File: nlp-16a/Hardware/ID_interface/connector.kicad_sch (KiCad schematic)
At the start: 8 parts

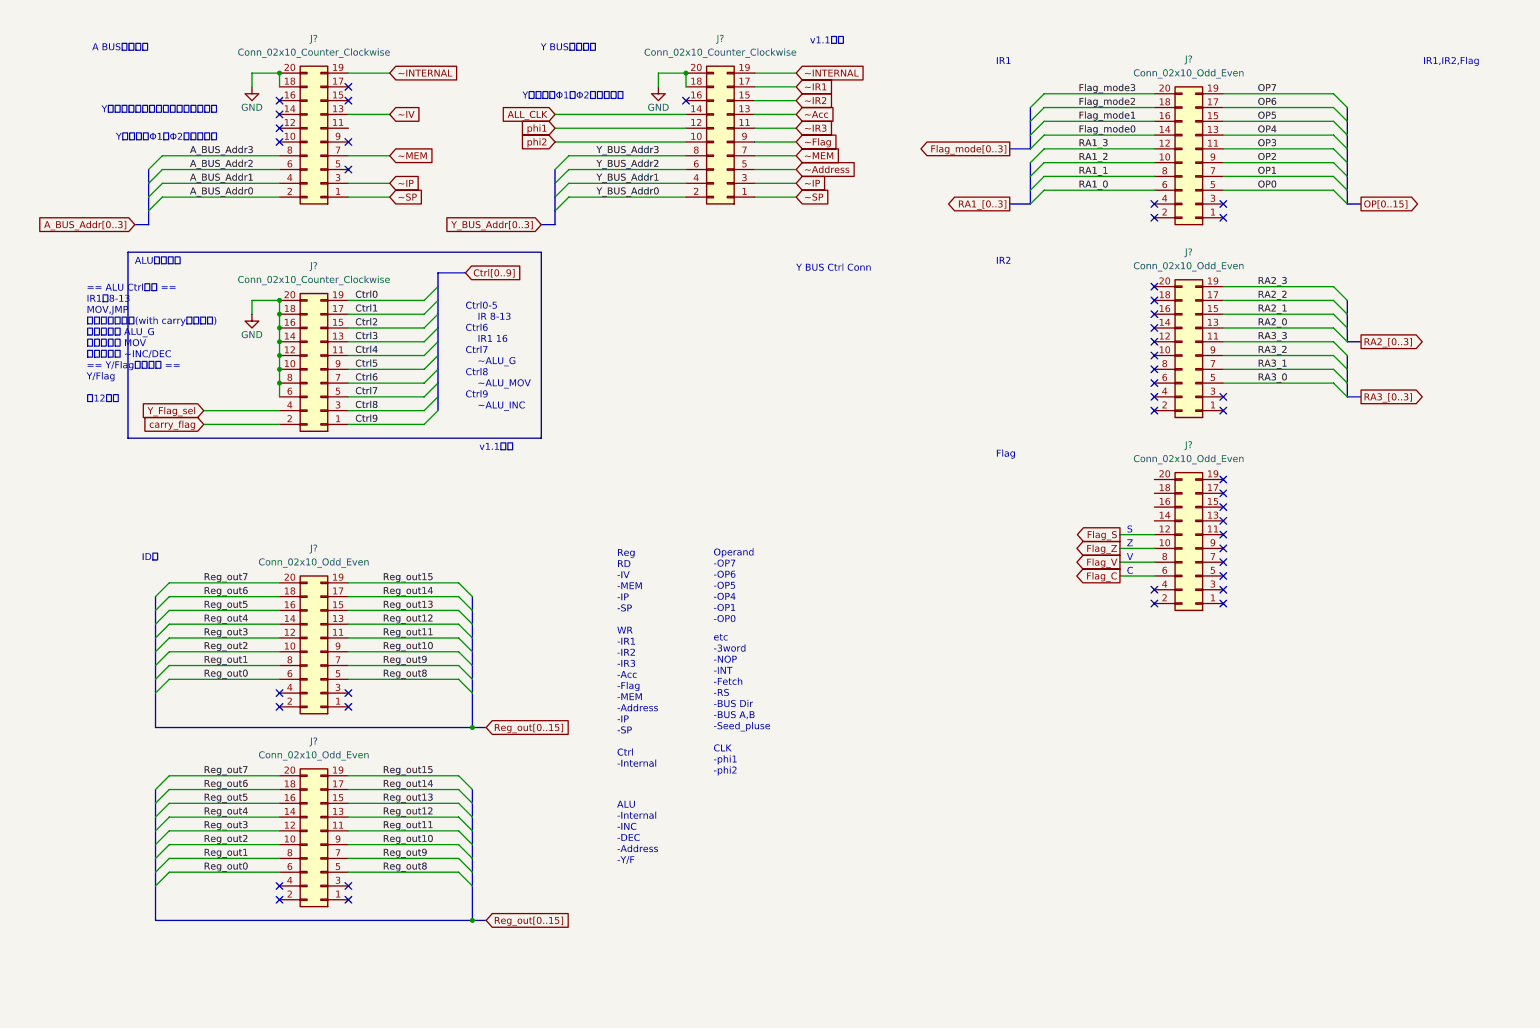
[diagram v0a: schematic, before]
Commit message: 命令デコーダとの配線方法を変更
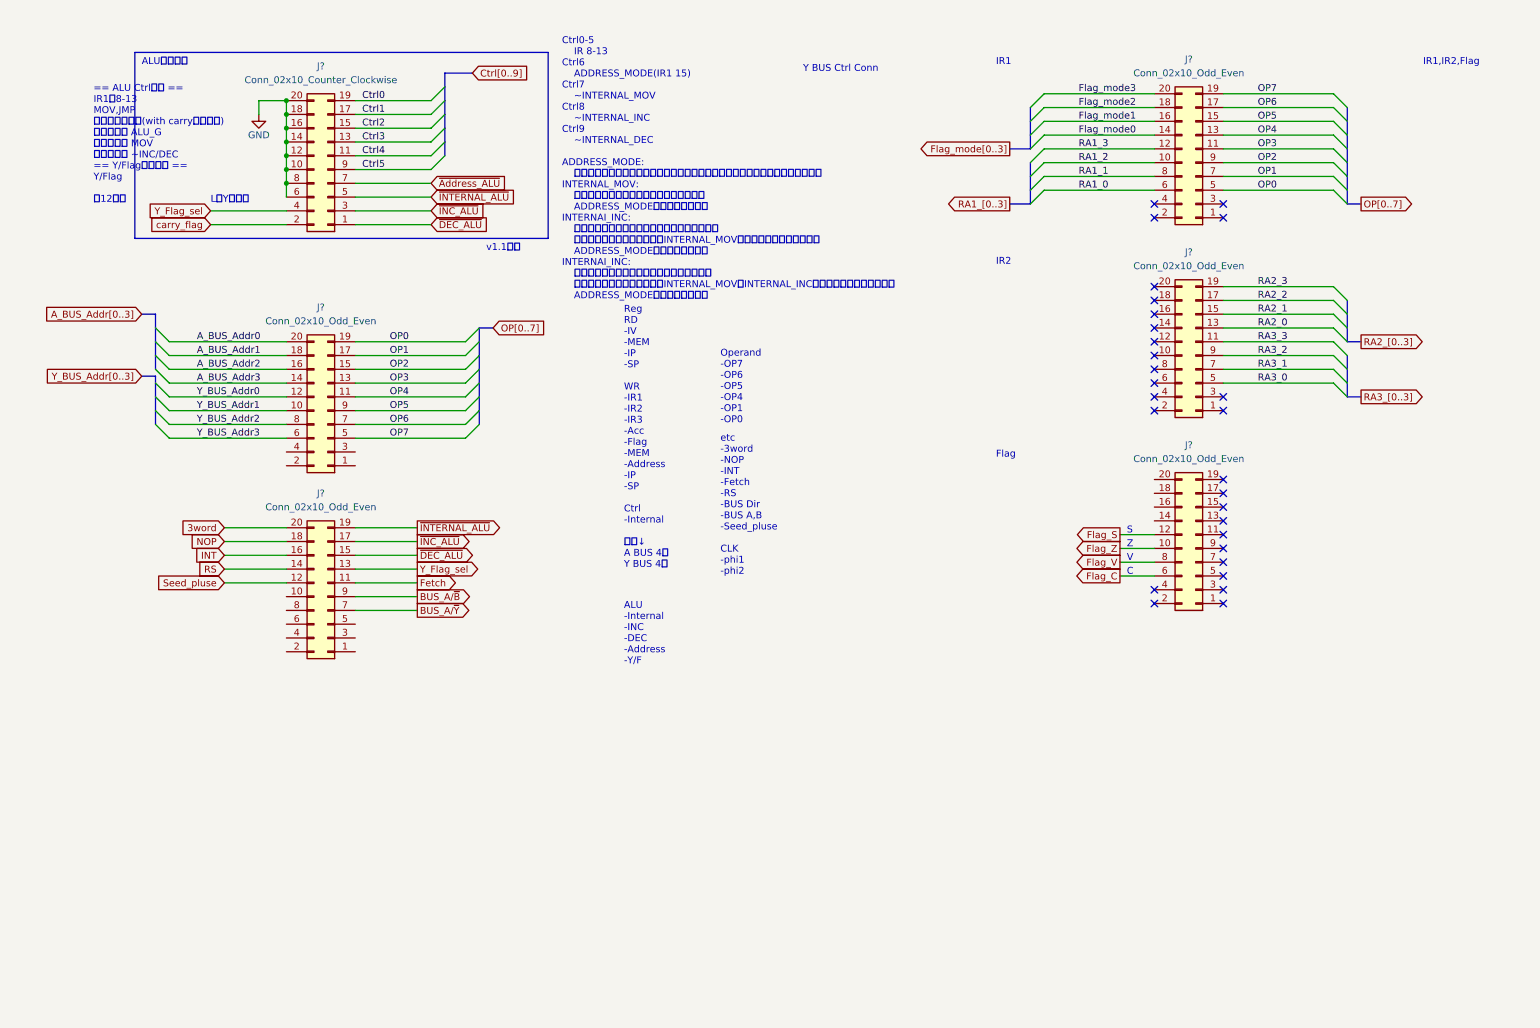
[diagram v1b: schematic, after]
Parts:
- removed J? (x2): Conn_02x10_Counter_Clockwise, Connector_PinHeader_2.54mm:PinHeader_2x10_P2.54mm_Horizontal, symbol Connector_Generic:Conn_02x10_Odd_Even
- removed J? (x2): Conn_02x10_Odd_Even, Connector_PinHeader_2.54mm:PinHeader_2x10_P2.54mm_Horizontal, symbol Connector_Generic:Conn_02x10_Odd_Even
- added J? (x2): Conn_02x10_Odd_Even, Connector_PinHeader_2.54mm:PinHeader_2x10_P2.54mm_Horizontal, symbol Connector_Generic:Conn_02x10_Odd_Even
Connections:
- net A_BUS_Addr0: now also J?.20 (Pin_20)
- net A_BUS_Addr1: now also J?.18 (Pin_18)
- net A_BUS_Addr2: now also J?.16 (Pin_16)
- net A_BUS_Addr3: now also J?.14 (Pin_14)
- net OP0: now also J?.19 (Pin_19)
- net OP1: now also J?.17 (Pin_17)
- net OP2: now also J?.15 (Pin_15)
- net OP3: now also J?.13 (Pin_13)
- net OP4: now also J?.11 (Pin_11)
- net OP5: now also J?.9 (Pin_9)
- net OP6: now also J?.7 (Pin_7)
- net OP7: now also J?.5 (Pin_5)
- net Y_BUS_Addr0: now also J?.12 (Pin_12)
- net Y_BUS_Addr1: now also J?.10 (Pin_10)
- net Y_BUS_Addr2: now also J?.8 (Pin_8)
- net Y_BUS_Addr3: now also J?.6 (Pin_6)
- net Y_Flag_sel: now also J?.13 (Pin_13)
- net Ctrl6 renamed ~{Address_ALU}
- net Ctrl7 renamed ~{INTERNAL_ALU}
- net ~{INTERNAL_ALU}: now also J?.19 (Pin_19)
- net Ctrl8 renamed ~{INC_ALU}
- net ~{INC_ALU}: now also J?.17 (Pin_17)
- net Ctrl9 renamed ~{DEC_ALU}
- net ~{DEC_ALU}: now also J?.15 (Pin_15)
- new net 3word: J?.20 (Pin_20)
- new net BUS_A/~{B}: J?.9 (Pin_9)
- new net BUS_A/~{Y}: J?.7 (Pin_7)
- new net Fetch: J?.11 (Pin_11)
- new net INT: J?.16 (Pin_16)
- new net NOP: J?.18 (Pin_18)
- new net RS: J?.14 (Pin_14)
- new net Seed_pluse: J?.12 (Pin_12)
- no-connect marks 45 -> 28
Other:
- note added: "Ctrl0-5 IR 8-13 Ctrl6 ADDRESS_MODE(IR1 15) Ctrl7 ~INTERNAL_MOV Ctrl8 ~INTERNAL_INC Ctrl9 ~INTERNAL_DEC ADDRESS_MODE: アドレッシング時の演算モードに切り替え．演算命令以外でこのモードになる． INTERNAL_MOV: 内部処理での値を移動するときのモード． ADDRESS_MODEより優先される． INTERNAI_INC: 内部処理でインクリメントするときのモード． このモードを使用する際にはINTERNAL_MOVが有効である必要がある． ADDRESS_MODEより優先される． INTERNAI_INC: 内部処理でデクリメントするときのモード． このモードを使用する際にはINTERNAL_MOV，INTERNAL_INCが有効である必要がある． ADDRESS_M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"
- note added: "LでYが出力"
- note added: "Reg RD -IV -MEM -IP -SP WR -IR1 -IR2 -IR3 -Acc -Flag -MEM -Address -IP -SP Ctrl -Internal 変更↓ A BUS 4本 Y BUS 4本"
- note removed: "A BUS制御バス"
- note removed: "Ctrl0-5 IR 8-13 Ctrl6 IR1 16 Ctrl7 ~ALU_G Ctrl8 ~ALU_MOV Ctrl9 ~ALU_INC"
- note removed: "IDへ"
- note removed: "Reg RD -IV -MEM -IP -SP WR -IR1 -IR2 -IR3 -Acc -Flag -MEM -Address -IP -SP Ctrl -Internal"
- note removed: "Y BUS制御バス"
- note removed: "YバスではΦ1，Φ2で使用する"
- note removed: "Yバスでは全レジスタ指定で使用する"
- moved on the sheet: J?

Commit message: 命令デコーダインターフェイスだいたい完了！！
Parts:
- removed J? (x2): Conn_02x10_Odd_Even, Connector_PinHeader_2.54mm:PinHeader_2x10_P2.54mm_Horizontal, symbol Connector_Generic:Conn_02x10_Odd_Even
- added C1, C10, C11, C12, C13, C14, C15, C16, C17, C18, C19, C2, C20, C21, C22, C3, C4, C5, C6, C7, C8, C9: C, Capacitor_THT:C_Disc_D7.0mm_W2.5mm_P5.00mm, symbol Device:C
- added C23: C_Polarized, Capacitor_THT:CP_Radial_D5.0mm_P2.50mm, symbol Device:C_Polarized
- added D1, D10, D11, D2, D3, D4, D5, D6, D7, D8, D9: LED, LED_THT:LED_D3.0mm, symbol Device:LED
- added H1, H2, H3, H4: MountingHole_Pad, MountingHole:MountingHole_3mm_Pad, symbol Mechanical:MountingHole_Pad
- added J1, J5, J6, J7, J8: Screw_Terminal_01x02, TerminalBlock:TerminalBlock_bornier-2_P5.08mm, symbol Connector:Screw_Terminal_01x02
- added J3, J4: Conn_02x10_Odd_Even, Connector_PinHeader_2.54mm:PinHeader_2x10_P2.54mm_Horizontal, symbol Connector_Generic:Conn_02x10_Odd_Even
- added R1, R2, R3: R, Resistor_SMD:R_0603_1608Metric_Pad0.98x0.95mm_HandSolder, symbol Device:R
- added RN1: R_Network08_Split, Resistor_THT:R_Array_SIP9, symbol Device:R_Network08_Split
- added U10: CD74HC00, Package_DIP:DIP-14_W7.62mm, symbol CD74HCxx:CD74HC00
- added U25, U26: CD74HC00, Package_DIP:DIP-14_W7.62mm, symbol CD74HCXX:CD74HC00
- gave numbers to parts that had none: 4
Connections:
- net Ctrl0 is gone; now on net OP5: J2.19 (Pin_19)
- net Ctrl1 is gone; now on net OP4: J2.17 (Pin_17)
- net Ctrl2 is gone; now on net OP3: J2.15 (Pin_15)
- net Ctrl3 is gone; now on net OP2: J2.13 (Pin_13)
- net Ctrl4 is gone; now on net OP1: J2.11 (Pin_11)
- net Ctrl5 is gone; now on net OP0: J2.9 (Pin_9)
- net carry_flag is gone; now on net Flag_C: J2.2 (Pin_2)
- net 3word: now also D4.2 (A), J4.8 (Pin_8)
- net A_BUS_Addr0: now also J3.12 (Pin_12)
- net A_BUS_Addr1: now also J3.10 (Pin_10)
- net A_BUS_Addr2: now also J3.8 (Pin_8)
- net A_BUS_Addr3: now also J3.6 (Pin_6)
- net BUS_A/~{B}: now also D11.2 (A), J4.9 (Pin_9)
- net BUS_A/~{Y}: now also D10.2 (A), J4.7 (Pin_7)
- net GND: now also C1.1, C10.1, C11.1, C12.1, C13.1, C14.1, C15.1, C16.1, C17.1, C18.1, C19.1, C2.1, C20.1, C21.1, C22.1, C23.2, C3.1, C4.1, C5.1, C6.1, C7.1, C8.1, C9.1, H1.1, H2.1, H3.1, H4.1, J1.1 (Pin_1), J3.2 (Pin_2), J3.4 (Pin_4), J4.2 (Pin_2), J4.4 (Pin_4), J5.1 (Pin_1), J6.1 (Pin_1), J7.1 (Pin_1), J8.1 (Pin_1), R1.2, R2.2, R3.2, RN1.1 (R1.1), U10.7 (GND), U25.7 (GND), U25.7 (GND), U25.7 (GND), U25.7 (GND), U26.7 (GND), U26.7 (GND), U26.7 (GND), U26.7 (GND)
- net INT: now also D6.2 (A), J4.10 (Pin_10)
- net NOP: now also D9.2 (A), J4.16 (Pin_16)
- net OP0: now also J3.19 (Pin_19)
- net OP1: now also J3.17 (Pin_17)
- net OP2: now also J3.15 (Pin_15)
- net OP3: now also J3.13 (Pin_13)
- net OP4: now also J3.11 (Pin_11)
- net OP5: now also J3.9 (Pin_9)
- net OP6: now also J3.7 (Pin_7)
- net OP7: now also J3.5 (Pin_5), U10.10, U10.9
- net RA1_0: now also J3.20 (Pin_20)
- net RA1_1: now also J3.18 (Pin_18)
- net RA1_2: now also J3.16 (Pin_16)
- net RA1_3: now also J3.14 (Pin_14)
- net Y_Flag_sel: now also J4.13 (Pin_13)
- net ~{DEC_ALU}: now also J4.15 (Pin_15)
- net ~{INC_ALU}: now also J4.17 (Pin_17)
- net ~{INTERNAL_ALU}: now also J4.19 (Pin_19)
- net ~{Address_ALU} renamed ~{Addr_ALU}
- net ~{Addr_ALU}: now also U10.8
- new net: D1.1 (K), R1.1
- new net: D8.1 (K), RN1.5 (R4.2)
- new net: D11.1 (K), RN1.2 (R1.2)
- new net: U26.10, U26.12, U26.13, U26.3, U26.4, U26.5, U26.9
- new net: U25.10, U25.12, U25.13, U25.3, U25.4, U25.5, U25.9
- new net: D2.2 (A), U25.11
- new net: D3.2 (A), U26.11
- new net: D3.1 (K), R3.1
- new net: D5.1 (K), RN1.8 (R7.2)
- new net: D2.1 (K), R2.1
- new net: D10.1 (K), RN1.3 (R2.2)
- new net: D9.1 (K), RN1.4 (R3.2)
- new net: D7.1 (K), RN1.6 (R5.2)
- new net: D4.1 (K), RN1.9 (R8.2)
- new net: D6.1 (K), RN1.7 (R6.2)
- new net INT_EN: D5.2 (A), J4.5 (Pin_5)
- new net VCC: C1.2, C10.2, C11.2, C12.2, C13.2, C14.2, C15.2, C16.2, C17.2, C18.2, C19.2, C2.2, C20.2, C21.2, C22.2, C23.1, C3.2, C4.2, C5.2, C6.2, C7.2, C8.2, C9.2, D1.2 (A), J1.2 (Pin_2), U10.14 (VCC), U25.14 (VCC), U25.14 (VCC), U25.14 (VCC), U25.14 (VCC), U26.14 (VCC), U26.14 (VCC), U26.14 (VCC), U26.14 (VCC)
- new net phi1: J5.2 (Pin_2), U25.1, U25.2
- new net phi1_1: J4.20 (Pin_20), U25.8
- new net phi1_2: U25.6
- new net phi2: J6.2 (Pin_2), U26.1, U26.2
- new net phi2_1: J4.18 (Pin_18), U26.8
- new net phi2_2: U26.6
- new net ~{Fetch_Status}: D7.2 (A), J4.11 (Pin_11)
- new net ~{INT_INPUT}: J8.2 (Pin_2)
- new net ~{RS}: D8.2 (A), J4.14 (Pin_14), J7.2 (Pin_2)
- new net ~{Seed_pluse}: J4.12 (Pin_12)
- no-connect marks 28 -> 37
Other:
- note added: "Power"
- note added: "Y BUS"
- note removed: "IR1,IR2,Flag"
- moved on the sheet: J10, J11, J9

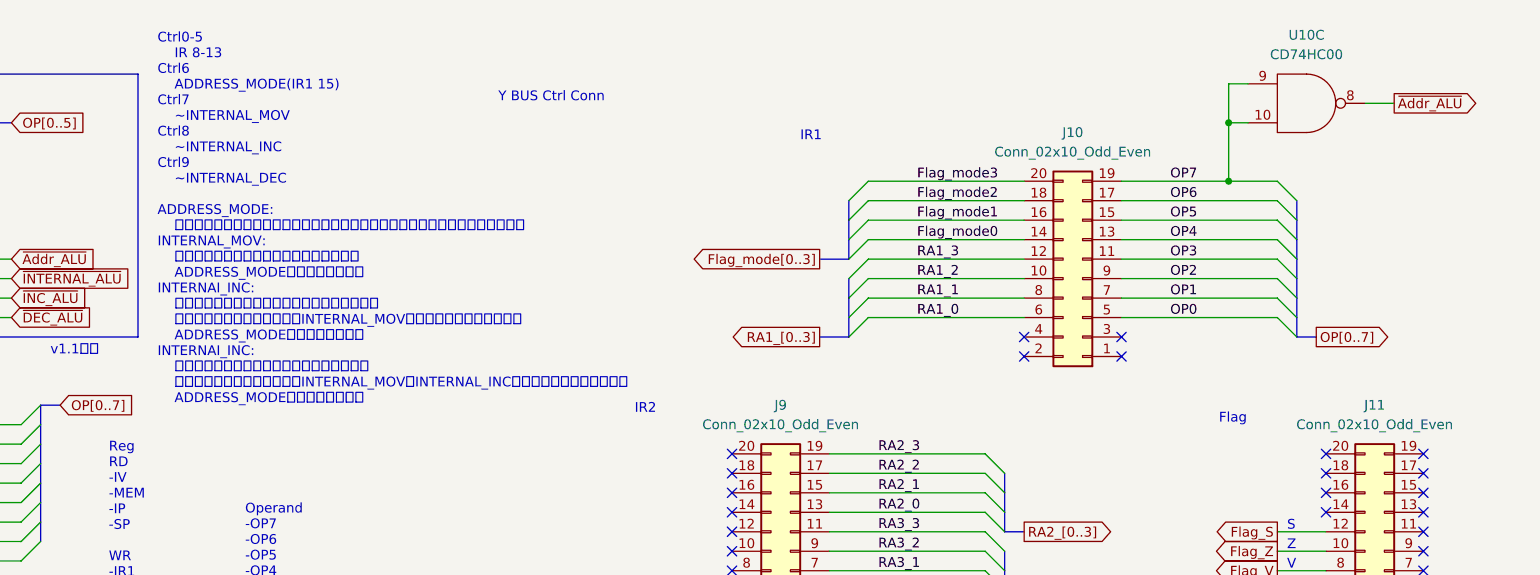
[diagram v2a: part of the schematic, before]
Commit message: 軽微な修正を加えてガーバー作成 発注
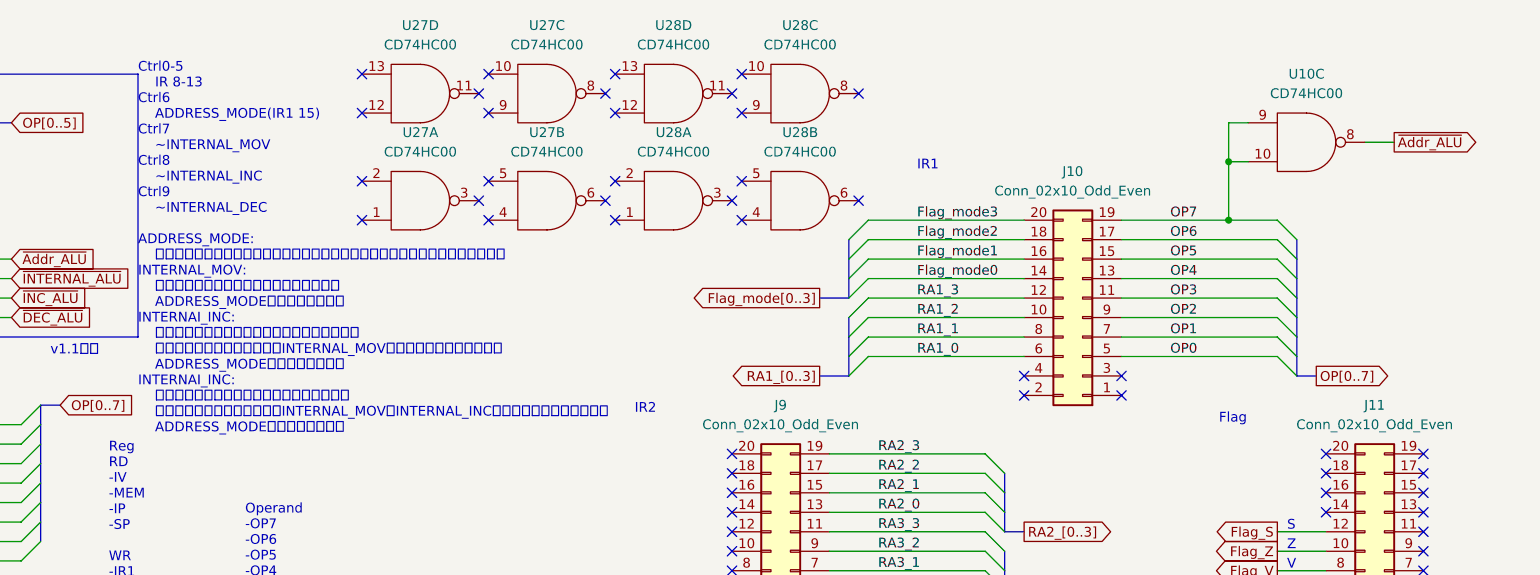
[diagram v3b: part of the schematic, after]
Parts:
- added U27, U28: CD74HC00, Package_DIP:DIP-14_W7.62mm, symbol CD74HCXX:CD74HC00
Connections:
- net GND: now also U27.7 (GND), U27.7 (GND), U27.7 (GND), U27.7 (GND), U28.7 (GND), U28.7 (GND), U28.7 (GND), U28.7 (GND)
- net VCC: now also U27.14 (VCC), U27.14 (VCC), U27.14 (VCC), U27.14 (VCC), U28.14 (VCC), U28.14 (VCC), U28.14 (VCC), U28.14 (VCC)
- no-connect marks 37 -> 61
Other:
- note removed: "Y BUS Ctrl Conn"
- moved on the sheet: J10, U10C
